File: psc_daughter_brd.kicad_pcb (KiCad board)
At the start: 2 copper layers, 50 x 150 mm, 144 parts, among them J1 61082-061400LF, U1 AD797, U11 ADR1001AEZ, U12 AD8221, U13 OPA277, U14 AD8221, U15 OPA277, U16 AD8221, U17 OPA277, U18 AD8221, U19 OPA277, U2 AD8676xR, U20 ADS8568SPM, U3 AD8676xR, U4 OPA277, U5 BUF634AxD, U6 AD5791BRUZ, U7 OPA277, U8 BUF634AxD, U9 OPA277

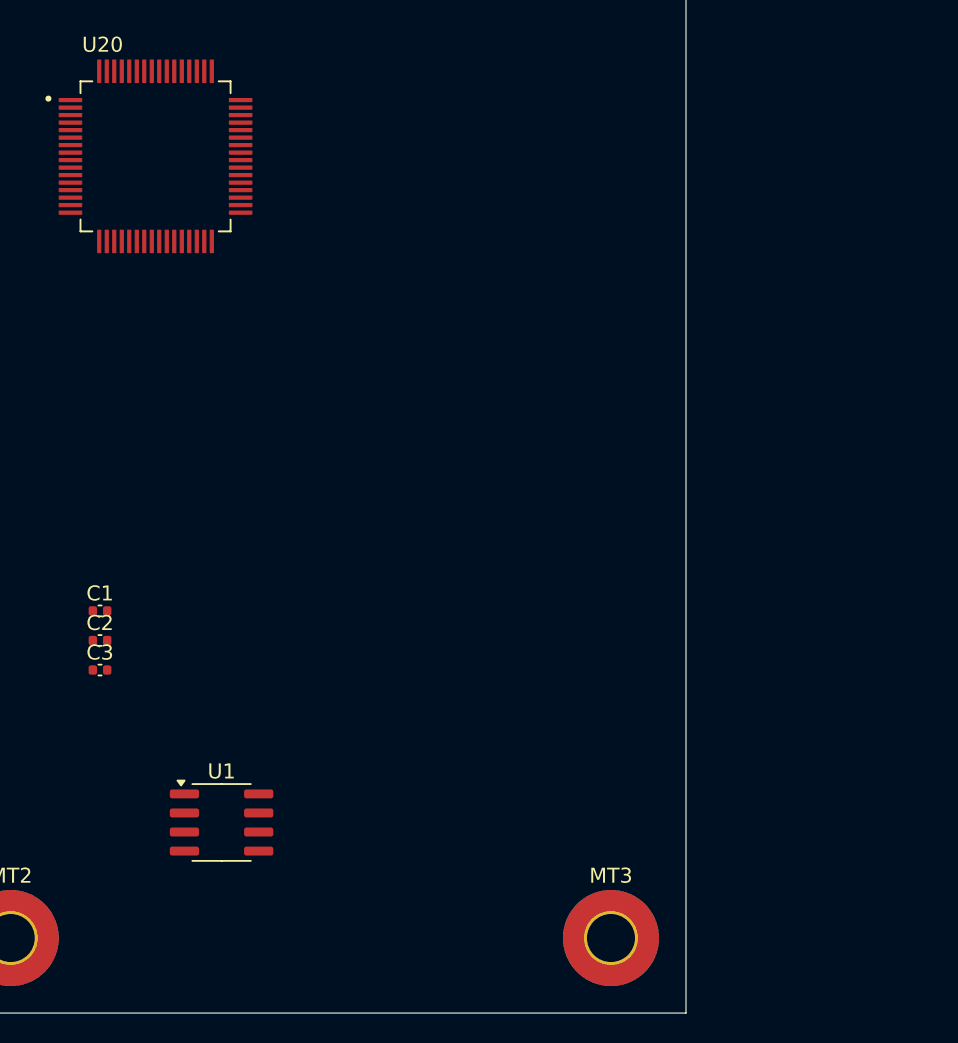
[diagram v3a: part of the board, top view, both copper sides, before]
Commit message: Add isolated digital I/O
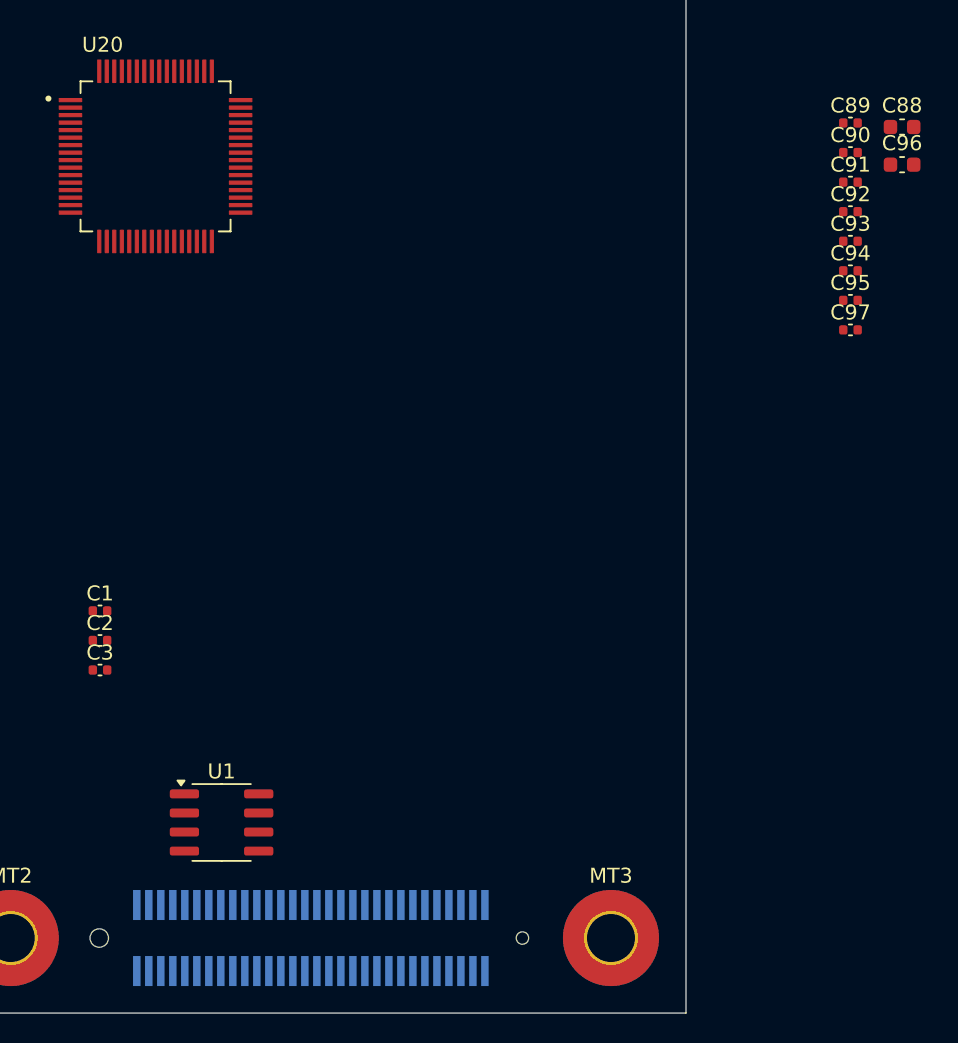
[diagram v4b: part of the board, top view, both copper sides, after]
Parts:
- added C88: 10uF, Capacitor_SMD:C_0603_1608Metric, F.Cu at (204.1, 132.7)
- added C89: 0.1uF, Capacitor_SMD:C_0402_1005Metric, F.Cu at (200.7, 132.5)
- added C90: 0.1uF, Capacitor_SMD:C_0402_1005Metric, F.Cu at (200.7, 134.4)
- added C91: 0.1uF, Capacitor_SMD:C_0402_1005Metric, F.Cu at (200.7, 136.4)
- added C92: 0.1uF, Capacitor_SMD:C_0402_1005Metric, F.Cu at (200.7, 138.4)
- added C93: 0.1uF, Capacitor_SMD:C_0402_1005Metric, F.Cu at (200.7, 140.3)
- added C94: 0.1uF, Capacitor_SMD:C_0402_1005Metric, F.Cu at (200.7, 142.3)
- added C95: 0.1uF, Capacitor_SMD:C_0402_1005Metric, F.Cu at (200.7, 144.3)
- added C96: 10uF, Capacitor_SMD:C_0603_1608Metric, F.Cu at (204.1, 135.2)
- added C97: 0.1uF, Capacitor_SMD:C_0402_1005Metric, F.Cu at (200.7, 146.2)
- added J2: 61082-061400LF, myparts:AMPHENOL_61082-061400LF, B.Cu at (164.7, 46.8)
- moved J1 140.0 mm to (164.7, 186.8)
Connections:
- net /DAC/SCLK renamed /DAC/sclk
- net /DAC/SDIN renamed /DAC/sdin
- net /DAC/SYNCN renamed /DAC/syncn
- U20 pad 10: unconnected-(U20-RESET-Pad10) -> /Monitor/reset
- U20 pad 11: unconnected-(U20-REFEN/~{WR}-Pad11) -> +3.3V
- U20 pad 12: unconnected-(U20-~{RD}-Pad12) -> GND
- U20 pad 13: unconnected-(U20-~{CS}/FS-Pad13) -> /Monitor/fs
- U20 pad 14: unconnected-(U20-AVDD-Pad14) -> Net-(C90-Pad1)
- U20 pad 15: unconnected-(U20-AGND-Pad15) -> GND
- U20 pad 16: unconnected-(U20-DB15/SDO_D-Pad16) -> GND
- U20 pad 17: unconnected-(U20-DB14/SDO_C-Pad17) -> GND
- U20 pad 18: unconnected-(U20-DB13/SDO_B-Pad18) -> GND
- U20 pad 19: unconnected-(U20-DB12/SDO_A-Pad19) -> /Monitor/sdo
- U20 pad 20: unconnected-(U20-DB11/~{REFBUFEN}-Pad20) -> GND
- U20 pad 21: unconnected-(U20-DB10/SCLK-Pad21) -> /Monitor/sclk
- U20 pad 22: unconnected-(U20-DB9/SDI-Pad22) -> GND
- U20 pad 23: unconnected-(U20-DB8/DCEN-Pad23) -> GND
- U20 pad 24: unconnected-(U20-DGND-Pad24) -> GND
- U20 pad 25: unconnected-(U20-DVDD-Pad25) -> +3.3V
- U20 pad 26: unconnected-(U20-DB7-Pad26) -> GND
- U20 pad 27: unconnected-(U20-DB6/SEL_B-Pad27) -> GND
- U20 pad 28: unconnected-(U20-DB5/SEL_CD-Pad28) -> GND
- U20 pad 29: unconnected-(U20-DB4-Pad29) -> GND
- U20 pad 30: unconnected-(U20-DB3/DCIN_A-Pad30) -> GND
- U20 pad 31: unconnected-(U20-DB2/DCIN_B-Pad31) -> GND
- U20 pad 32: unconnected-(U20-DB1/DCIN_C-Pad32) -> GND
- U20 pad 33: unconnected-(U20-DB0/DCIN_D-Pad33) -> GND
- U20 pad 34: unconnected-(U20-RANGE/XCLK-Pad34) -> GND
- U20 pad 35: unconnected-(U20-BUSY/INT-Pad35) -> /Monitor/busy
- U20 pad 36: unconnected-(U20-ASLEEP-Pad36) -> GND
- U20 pad 37: unconnected-(U20-CONVST_A-Pad37) -> /Monitor/convert
- U20 pad 38: unconnected-(U20-CONVST_B-Pad38) -> /Monitor/convert
- U20 pad 39: unconnected-(U20-CONVST_C-Pad39) -> /Monitor/convert
- U20 pad 4: unconnected-(U20-AVDD-Pad4) -> Net-(C90-Pad1)
- U20 pad 40: unconnected-(U20-CONVST_D-Pad40) -> /Monitor/convert
- U20 pad 41: unconnected-(U20-~{HW}/SW-Pad41) -> GND
- U20 pad 44: unconnected-(U20-AGND-Pad44) -> GND
- U20 pad 45: unconnected-(U20-AVDD-Pad45) -> Net-(C90-Pad1)
- U20 pad 48: unconnected-(U20-HVDD-Pad48) -> +15V
- U20 pad 5: unconnected-(U20-AGND-Pad5) -> GND
- U20 pad 51: unconnected-(U20-AGND-Pad51) -> GND
- U20 pad 52: unconnected-(U20-AVDD-Pad52) -> Net-(C90-Pad1)
- U20 pad 57: unconnected-(U20-AVDD-Pad57) -> Net-(C90-Pad1)
- U20 pad 58: unconnected-(U20-AGND-Pad58) -> GND
- U20 pad 61: unconnected-(U20-AVDD-Pad61) -> Net-(C90-Pad1)
- U20 pad 62: unconnected-(U20-AGND-Pad62) -> GND
- U20 pad 8: unconnected-(U20-~{PAR}/SER-Pad8) -> +3.3V
- U20 pad 9: unconnected-(U20-~{STBY}-Pad9) -> +3.3V

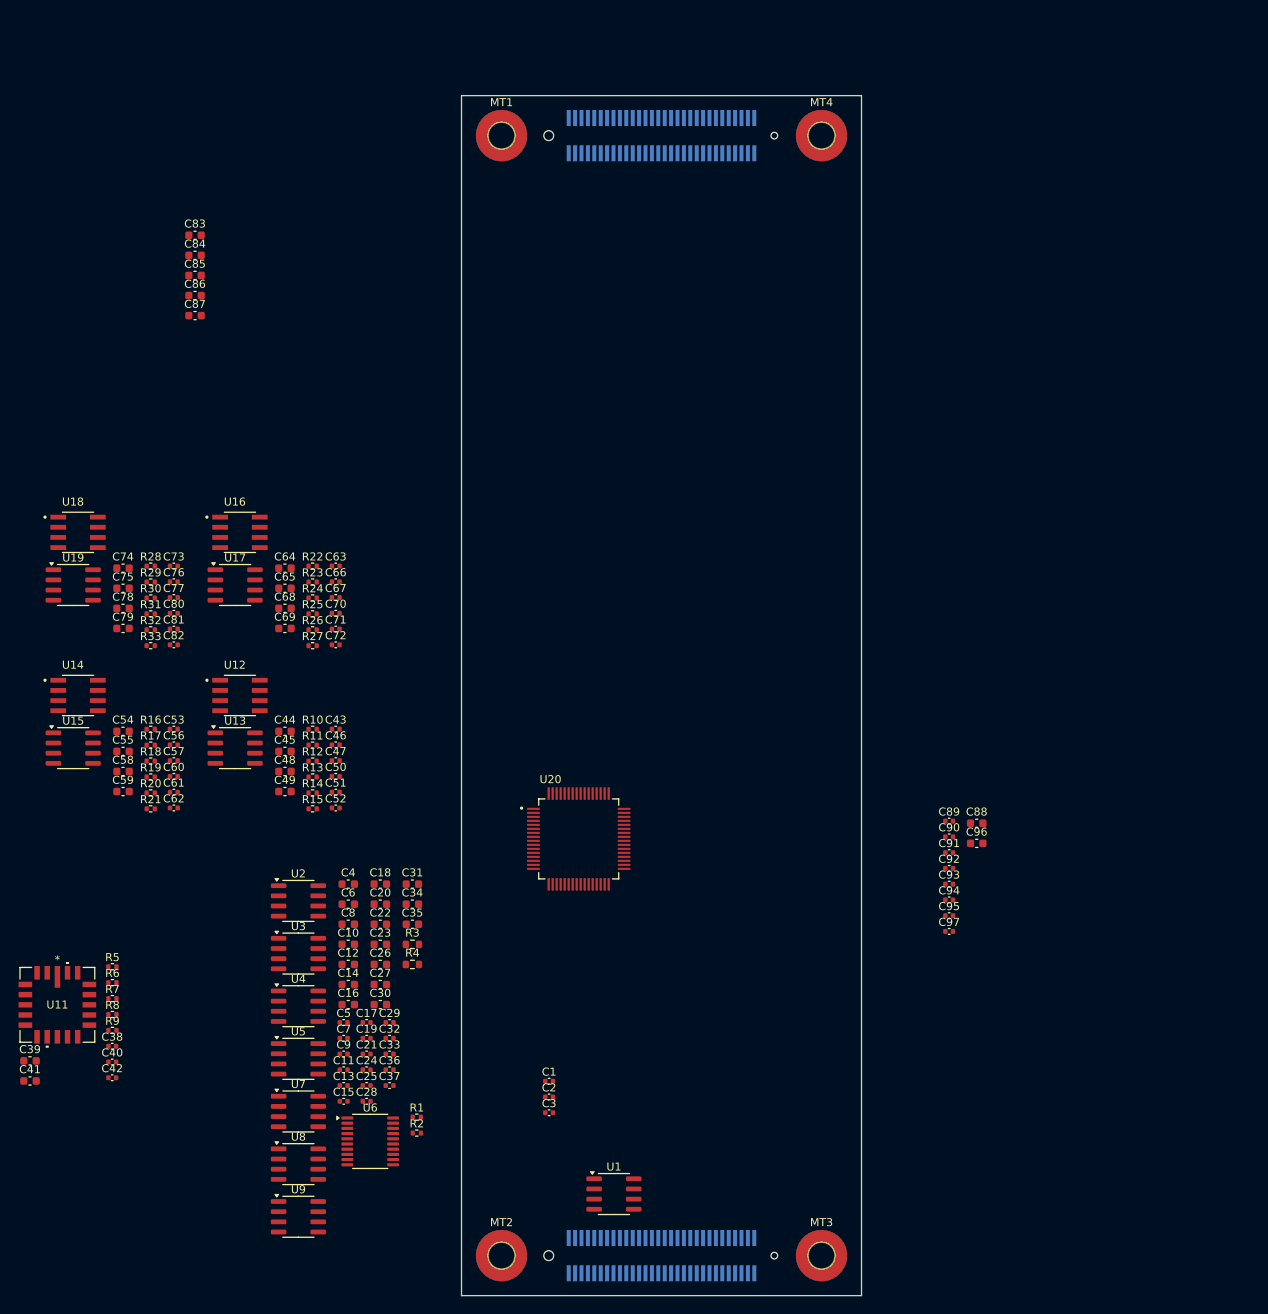
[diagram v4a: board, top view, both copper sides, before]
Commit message: Add DCCT ADCs
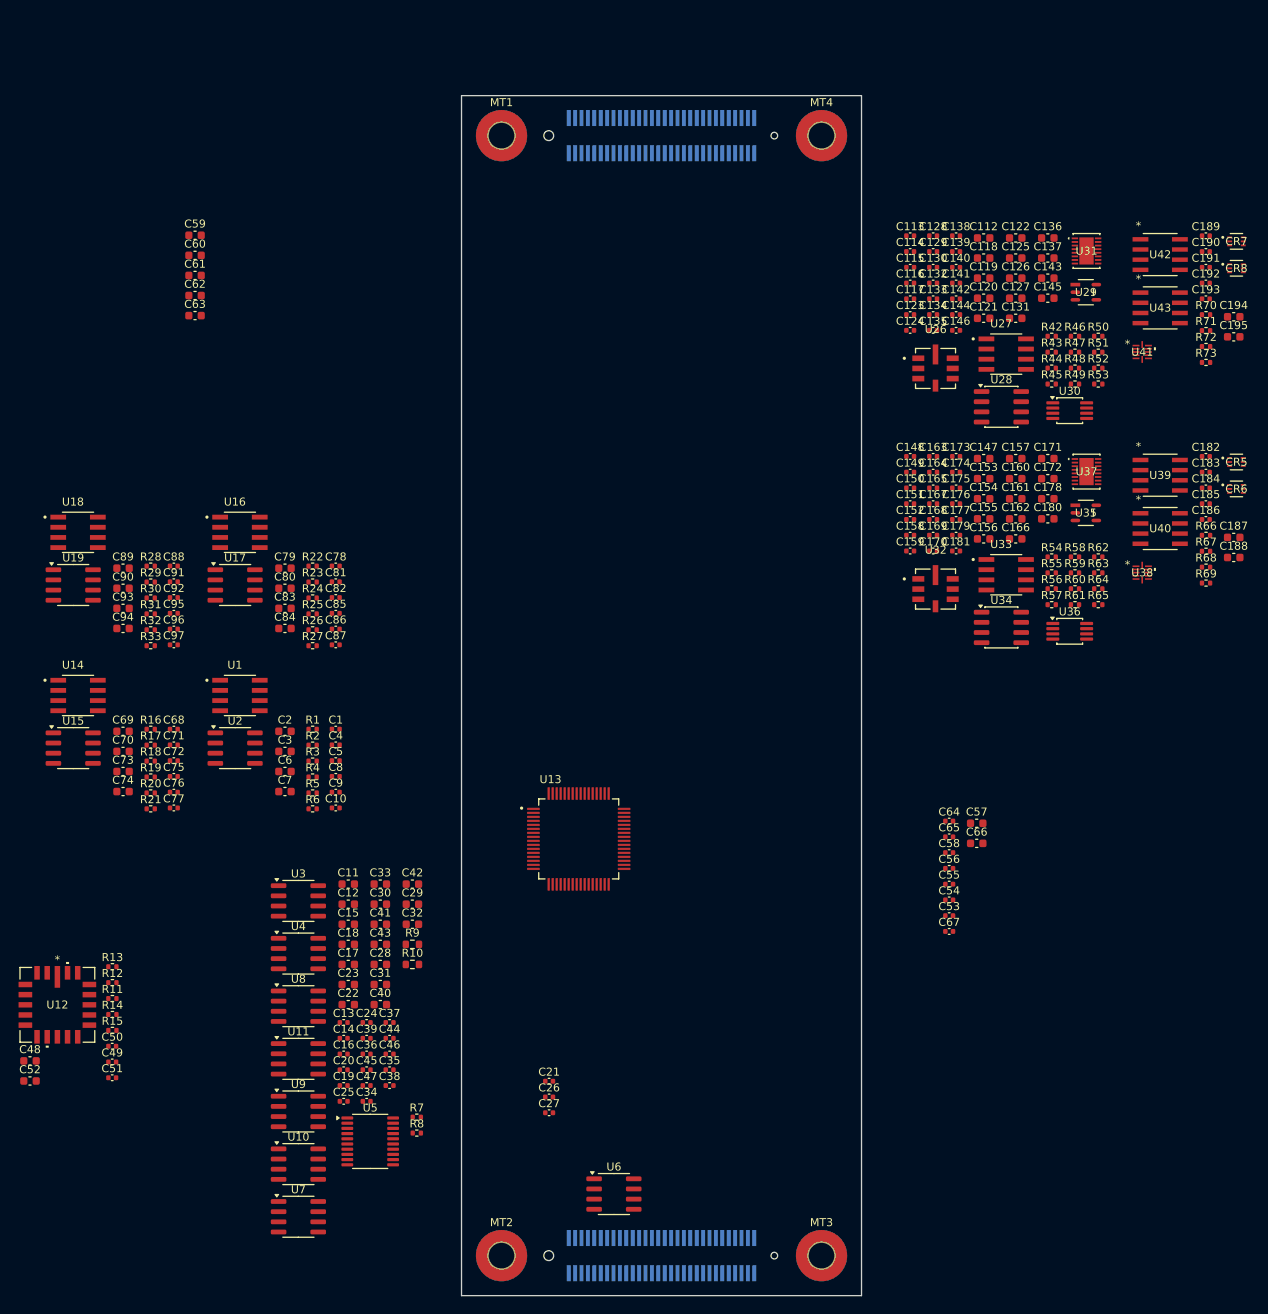
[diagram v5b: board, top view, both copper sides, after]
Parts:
- added C112: 10uF, Capacitor_SMD:C_0603_1608Metric, F.Cu at (205.0, 59.6)
- added C113: 0.1uF, Capacitor_SMD:C_0402_1005Metric, F.Cu at (195.8, 59.3)
- added C114: 6800pF, Capacitor_SMD:C_0402_1005Metric, F.Cu at (195.8, 61.3)
- added C115: 6800pF, Capacitor_SMD:C_0402_1005Metric, F.Cu at (195.8, 63.2)
- added C116: 3300pF, Capacitor_SMD:C_0402_1005Metric, F.Cu at (195.8, 65.2)
- added C117: 0.1uF, Capacitor_SMD:C_0402_1005Metric, F.Cu at (195.8, 67.2)
- added C118: 10uF, Capacitor_SMD:C_0603_1608Metric, F.Cu at (205.0, 62.1)
- added C119: 10uF, Capacitor_SMD:C_0603_1608Metric, F.Cu at (205.0, 64.6)
- added C120: 10uF, Capacitor_SMD:C_0603_1608Metric, F.Cu at (205.0, 67.1)
- added C121: 10uF, Capacitor_SMD:C_0603_1608Metric, F.Cu at (205.0, 69.6)
- added C122: 10uF, Capacitor_SMD:C_0603_1608Metric, F.Cu at (209.0, 59.6)
- added C123: 0.1uF, Capacitor_SMD:C_0402_1005Metric, F.Cu at (195.8, 69.1)
- added C124: 0.01uF, Capacitor_SMD:C_0402_1005Metric, F.Cu at (195.8, 71.1)
- added C125: 10uF, Capacitor_SMD:C_0603_1608Metric, F.Cu at (209.0, 62.1)
- added C126: 10uF, Capacitor_SMD:C_0603_1608Metric, F.Cu at (209.0, 64.6)
- added C127: 10uF, Capacitor_SMD:C_0603_1608Metric, F.Cu at (209.0, 67.1)
- added C128: 0.1uF, Capacitor_SMD:C_0402_1005Metric, F.Cu at (198.7, 59.3)
- added C129: 0.1uF, Capacitor_SMD:C_0402_1005Metric, F.Cu at (198.7, 61.3)
- added C130: 0.1uF, Capacitor_SMD:C_0402_1005Metric, F.Cu at (198.7, 63.2)
- added C131: 10uF, Capacitor_SMD:C_0603_1608Metric, F.Cu at (209.0, 69.6)
- added C132: 6800pF, Capacitor_SMD:C_0402_1005Metric, F.Cu at (198.7, 65.2)
- added C133: 3300pF, Capacitor_SMD:C_0402_1005Metric, F.Cu at (198.7, 67.2)
- added C134: 6800pF, Capacitor_SMD:C_0402_1005Metric, F.Cu at (198.7, 69.1)
- added C135: 0.1uF, Capacitor_SMD:C_0402_1005Metric, F.Cu at (198.7, 71.1)
- added C136: 10uF, Capacitor_SMD:C_0603_1608Metric, F.Cu at (213.0, 59.6)
- added C137: 10uF, Capacitor_SMD:C_0603_1608Metric, F.Cu at (213.0, 62.1)
- added C138: 0.1uF, Capacitor_SMD:C_0402_1005Metric, F.Cu at (201.5, 59.3)
- added C139: 0.1uF, Capacitor_SMD:C_0402_1005Metric, F.Cu at (201.5, 61.3)
- added C140: 6800pF, Capacitor_SMD:C_0402_1005Metric, F.Cu at (201.5, 63.2)
- added C141: 3300pF, Capacitor_SMD:C_0402_1005Metric, F.Cu at (201.5, 65.2)
- added C142: 6800pF, Capacitor_SMD:C_0402_1005Metric, F.Cu at (201.5, 67.2)
- added C143: 10uF, Capacitor_SMD:C_0603_1608Metric, F.Cu at (213.0, 64.6)
- added C144: 0.1uF, Capacitor_SMD:C_0402_1005Metric, F.Cu at (201.5, 69.1)
- added C145: 10uF, Capacitor_SMD:C_0603_1608Metric, F.Cu at (213.0, 67.1)
- added C146: 0.1uF, Capacitor_SMD:C_0402_1005Metric, F.Cu at (201.5, 71.1)
- added C147: 10uF, Capacitor_SMD:C_0603_1608Metric, F.Cu at (205.0, 87.1)
- added C148: 0.1uF, Capacitor_SMD:C_0402_1005Metric, F.Cu at (195.8, 86.9)
- added C149: 6800pF, Capacitor_SMD:C_0402_1005Metric, F.Cu at (195.8, 88.8)
- added C150: 6800pF, Capacitor_SMD:C_0402_1005Metric, F.Cu at (195.8, 90.8)
- added C151: 3300pF, Capacitor_SMD:C_0402_1005Metric, F.Cu at (195.8, 92.8)
- added C152: 0.1uF, Capacitor_SMD:C_0402_1005Metric, F.Cu at (195.8, 94.8)
- added C153: 10uF, Capacitor_SMD:C_0603_1608Metric, F.Cu at (205.0, 89.7)
- added C154: 10uF, Capacitor_SMD:C_0603_1608Metric, F.Cu at (205.0, 92.2)
- added C155: 10uF, Capacitor_SMD:C_0603_1608Metric, F.Cu at (205.0, 94.7)
- added C156: 10uF, Capacitor_SMD:C_0603_1608Metric, F.Cu at (205.0, 97.2)
- added C157: 10uF, Capacitor_SMD:C_0603_1608Metric, F.Cu at (209.0, 87.1)
- added C158: 0.1uF, Capacitor_SMD:C_0402_1005Metric, F.Cu at (195.8, 96.7)
- added C159: 0.01uF, Capacitor_SMD:C_0402_1005Metric, F.Cu at (195.8, 98.7)
- added C160: 10uF, Capacitor_SMD:C_0603_1608Metric, F.Cu at (209.0, 89.7)
- added C161: 10uF, Capacitor_SMD:C_0603_1608Metric, F.Cu at (209.0, 92.2)
- added C162: 10uF, Capacitor_SMD:C_0603_1608Metric, F.Cu at (209.0, 94.7)
- added C163: 0.1uF, Capacitor_SMD:C_0402_1005Metric, F.Cu at (198.7, 86.9)
- added C164: 0.1uF, Capacitor_SMD:C_0402_1005Metric, F.Cu at (198.7, 88.8)
- added C165: 0.1uF, Capacitor_SMD:C_0402_1005Metric, F.Cu at (198.7, 90.8)
- added C166: 10uF, Capacitor_SMD:C_0603_1608Metric, F.Cu at (209.0, 97.2)
- added C167: 6800pF, Capacitor_SMD:C_0402_1005Metric, F.Cu at (198.7, 92.8)
- added C168: 3300pF, Capacitor_SMD:C_0402_1005Metric, F.Cu at (198.7, 94.8)
- added C169: 6800pF, Capacitor_SMD:C_0402_1005Metric, F.Cu at (198.7, 96.7)
- added C170: 0.1uF, Capacitor_SMD:C_0402_1005Metric, F.Cu at (198.7, 98.7)
- added C171: 10uF, Capacitor_SMD:C_0603_1608Metric, F.Cu at (213.0, 87.1)
- added C172: 10uF, Capacitor_SMD:C_0603_1608Metric, F.Cu at (213.0, 89.7)
- added C173: 0.1uF, Capacitor_SMD:C_0402_1005Metric, F.Cu at (201.5, 86.9)
- added C174: 0.1uF, Capacitor_SMD:C_0402_1005Metric, F.Cu at (201.5, 88.8)
- added C175: 6800pF, Capacitor_SMD:C_0402_1005Metric, F.Cu at (201.5, 90.8)
- added C176: 3300pF, Capacitor_SMD:C_0402_1005Metric, F.Cu at (201.5, 92.8)
- added C177: 6800pF, Capacitor_SMD:C_0402_1005Metric, F.Cu at (201.5, 94.8)
- added C178: 10uF, Capacitor_SMD:C_0603_1608Metric, F.Cu at (213.0, 92.2)
- added C179: 0.1uF, Capacitor_SMD:C_0402_1005Metric, F.Cu at (201.5, 96.7)
- added C180: 10uF, Capacitor_SMD:C_0603_1608Metric, F.Cu at (213.0, 94.7)
- added C181: 0.1uF, Capacitor_SMD:C_0402_1005Metric, F.Cu at (201.5, 98.7)
- added C182: 0.1uF, Capacitor_SMD:C_0402_1005Metric, F.Cu at (232.7, 86.9)
- added C183: 0.1uF, Capacitor_SMD:C_0402_1005Metric, F.Cu at (232.7, 88.8)
- added C184: 0.1uF, Capacitor_SMD:C_0402_1005Metric, F.Cu at (232.7, 90.8)
- added C185: 0.1uF, Capacitor_SMD:C_0402_1005Metric, F.Cu at (232.7, 92.8)
- added C186: 0.1uF, Capacitor_SMD:C_0402_1005Metric, F.Cu at (232.7, 94.8)
- added C187: 10uF, Capacitor_SMD:C_0603_1608Metric, F.Cu at (236.2, 97.0)
- added C188: 10uF, Capacitor_SMD:C_0603_1608Metric, F.Cu at (236.2, 99.5)
- added C189: 0.1uF, Capacitor_SMD:C_0402_1005Metric, F.Cu at (232.7, 59.3)
- added C190: 0.1uF, Capacitor_SMD:C_0402_1005Metric, F.Cu at (232.7, 61.3)
- added C191: 0.1uF, Capacitor_SMD:C_0402_1005Metric, F.Cu at (232.7, 63.2)
- added C192: 0.1uF, Capacitor_SMD:C_0402_1005Metric, F.Cu at (232.7, 65.2)
- added C193: 0.1uF, Capacitor_SMD:C_0402_1005Metric, F.Cu at (232.7, 67.2)
- added C194: 10uF, Capacitor_SMD:C_0603_1608Metric, F.Cu at (236.2, 69.4)
- added C195: 10uF, Capacitor_SMD:C_0603_1608Metric, F.Cu at (236.2, 71.9)
- added CR5: SP3006-02XTG, myparts:SOT563_LTF, F.Cu at (236.6, 87.6)
- added CR6: SP3006-02XTG, myparts:SOT563_LTF, F.Cu at (236.6, 90.9)
- added CR7: SP3006-02XTG, myparts:SOT563_LTF, F.Cu at (236.6, 60.0)
- added CR8: SP3006-02XTG, myparts:SOT563_LTF, F.Cu at (236.6, 63.3)
- added R42: 1.0K, Resistor_SMD:R_0402_1005Metric, F.Cu at (213.5, 71.8)
- added R43: 1.0K, Resistor_SMD:R_0402_1005Metric, F.Cu at (213.5, 73.8)
- added R44: 665, Resistor_SMD:R_0402_1005Metric, F.Cu at (213.5, 75.8)
- added R45: 0, Resistor_SMD:R_0402_1005Metric, F.Cu at (213.5, 77.8)
- added R46: 1.3K, Resistor_SMD:R_0402_1005Metric, F.Cu at (216.4, 71.8)
- added R47: 10K, Resistor_SMD:R_0402_1005Metric, F.Cu at (216.4, 73.8)
- added R48: 10K, Resistor_SMD:R_0402_1005Metric, F.Cu at (216.4, 75.8)
- added R49: 10, Resistor_SMD:R_0402_1005Metric, F.Cu at (216.4, 77.8)
- added R50: 10, Resistor_SMD:R_0402_1005Metric, F.Cu at (219.3, 71.8)
- added R51: 15, Resistor_SMD:R_0402_1005Metric, F.Cu at (219.3, 73.8)
- added R52: 30.1, Resistor_SMD:R_0402_1005Metric, F.Cu at (219.3, 75.8)
- added R53: 30.1, Resistor_SMD:R_0402_1005Metric, F.Cu at (219.3, 77.8)
- added R54: 1.0K, Resistor_SMD:R_0402_1005Metric, F.Cu at (213.5, 99.4)
- added R55: 1.0K, Resistor_SMD:R_0402_1005Metric, F.Cu at (213.5, 101.4)
- added R56: 665, Resistor_SMD:R_0402_1005Metric, F.Cu at (213.5, 103.4)
- added R57: 0, Resistor_SMD:R_0402_1005Metric, F.Cu at (213.5, 105.4)
- added R58: 1.3K, Resistor_SMD:R_0402_1005Metric, F.Cu at (216.4, 99.4)
- added R59: 10K, Resistor_SMD:R_0402_1005Metric, F.Cu at (216.4, 101.4)
- added R60: 10K, Resistor_SMD:R_0402_1005Metric, F.Cu at (216.4, 103.4)
- added R61: 10, Resistor_SMD:R_0402_1005Metric, F.Cu at (216.4, 105.4)
- added R62: 10, Resistor_SMD:R_0402_1005Metric, F.Cu at (219.3, 99.4)
- added R63: 15, Resistor_SMD:R_0402_1005Metric, F.Cu at (219.3, 101.4)
- added R64: 30.1, Resistor_SMD:R_0402_1005Metric, F.Cu at (219.3, 103.4)
- added R65: 30.1, Resistor_SMD:R_0402_1005Metric, F.Cu at (219.3, 105.4)
- added R66: 2.49K, Resistor_SMD:R_0402_1005Metric, F.Cu at (232.8, 96.7)
- added R67: 2.49K, Resistor_SMD:R_0402_1005Metric, F.Cu at (232.8, 98.7)
- added R68: 2.49K, Resistor_SMD:R_0402_1005Metric, F.Cu at (232.8, 100.7)
- added R69: 2.49K, Resistor_SMD:R_0402_1005Metric, F.Cu at (232.8, 102.7)
- added R70: 2.49K, Resistor_SMD:R_0402_1005Metric, F.Cu at (232.8, 69.2)
- added R71: 2.49K, Resistor_SMD:R_0402_1005Metric, F.Cu at (232.8, 71.1)
- added R72: 2.49K, Resistor_SMD:R_0402_1005Metric, F.Cu at (232.8, 73.1)
- added R73: 2.49K, Resistor_SMD:R_0402_1005Metric, F.Cu at (232.8, 75.1)
- added U26: LTC6655BHLS8-5, myparts:LTC6655, F.Cu at (198.9, 75.9)
- added U27: AD8429BRZ, myparts:SOIC127P600X175-8N, F.Cu at (207.8, 74.1)
- added U28: AD8675ARZ, Package_SO:SOIC-8_3.9x4.9mm_P1.27mm, F.Cu at (207.2, 80.7)
- added U29: LT6202CS5, myparts:LT6202CS5, F.Cu at (217.7, 66.3)
- added U30: LTC6363xMS8, Package_SO:MSOP-8_3x3mm_P0.65mm, F.Cu at (215.7, 81.1)
- added U31: LTC2376CDE-20-PBF, myparts:DFN-16_DE_LIT, F.Cu at (217.8, 61.2)
- added U32: LTC6655BHLS8-5, myparts:LTC6655, F.Cu at (198.9, 103.5)
- added U33: AD8429BRZ, myparts:SOIC127P600X175-8N, F.Cu at (207.8, 101.7)
- added U34: AD8675ARZ, Package_SO:SOIC-8_3.9x4.9mm_P1.27mm, F.Cu at (207.2, 108.2)
- added U35: LT6202CS5, myparts:LT6202CS5, F.Cu at (217.7, 93.9)
- added U36: LTC6363xMS8, Package_SO:MSOP-8_3x3mm_P0.65mm, F.Cu at (215.7, 108.7)
- added U37: LTC2376CDE-20-PBF, myparts:DFN-16_DE_LIT, F.Cu at (217.8, 88.8)
- added U38: TXUN0104RUTR, myparts:PQFP12_RUT_TEX, F.Cu at (224.8, 101.4)
- added U39: ADUM5240ARZ, myparts:R_8_ADI, F.Cu at (227.0, 89.2)
- added U40: ADUM5240ARZ, myparts:R_8_ADI, F.Cu at (227.0, 95.9)
- added U41: TXUN0104RUTR, myparts:PQFP12_RUT_TEX, F.Cu at (224.8, 73.8)
- added U42: ADUM5242ARZ, myparts:R_8_ADI, F.Cu at (227.0, 61.6)
- added U43: ADUM5242ARZ, myparts:R_8_ADI, F.Cu at (227.0, 68.3)
- renumbered C43 to C1, C52 to C10, C4 to C11, C6 to C12, C5 to C13, C7 to C14, C8 to C15, C9 to C16, C12 to C17, C10 to C18, C13 to C19, C44 to C2, C11 to C20, C1 to C21, C16 to C22, C14 to C23, C17 to C24, C15 to C25, C2 to C26, C3 to C27, C26 to C28, C34 to C29, C45 to C3, C20 to C30, C27 to C31, C35 to C32, C18 to C33, C28 to C34, C36 to C35, C21 to C36, C29 to C37, C37 to C38, C19 to C39, C46 to C4, C30 to C40, C22 to C41, C31 to C42, C23 to C43, C32 to C44, C24 to C45, C33 to C46, C25 to C47, C39 to C48, C40 to C49, C47 to C5, C38 to C50, C42 to C51, C41 to C52, C95 to C53, C94 to C54, C93 to C55, C92 to C56, C88 to C57, C91 to C58, C83 to C59, C48 to C6, C84 to C60, C85 to C61, C86 to C62, C87 to C63, C89 to C64, C90 to C65, C96 to C66, C97 to C67, C53 to C68, C54 to C69, C49 to C7, C55 to C70, C56 to C71, C57 to C72, C58 to C73, C59 to C74, C60 to C75, C61 to C76, C62 to C77, C63 to C78, C64 to C79, C50 to C8, C65 to C80, C66 to C81, C67 to C82, C68 to C83, C69 to C84, C70 to C85, C71 to C86, C72 to C87, C73 to C88, C74 to C89, C51 to C9, C75 to C90, C76 to C91, C77 to C92, C78 to C93, C79 to C94, C80 to C95, C81 to C96, C82 to C97, J2 to J1, J1 to J2, R10 to R1, R4 to R10, R7 to R11, R6 to R12, R5 to R13, R8 to R14, R9 to R15, R11 to R2, R12 to R3, R13 to R4, R14 to R5, R15 to R6, R1 to R7, R2 to R8, R3 to R9, U12 to U1, U8 to U10, U5 to U11, U11 to U12, U20 to U13, U13 to U2, U2 to U3, U3 to U4, U6 to U5, U1 to U6, U9 to U7, U4 to U8, U7 to U9
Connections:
- net /Monitor/busy renamed /Monitor ADCs/busy
- net /Monitor/convert renamed /Monitor ADCs/convert
- net /Monitor/fs renamed /Monitor ADCs/fs
- net /Monitor/monitor_dac/mon_out renamed /Monitor ADCs/monitor_dac/mon_out
- net /Monitor/monitor_ignd/mon_out renamed /Monitor ADCs/monitor_ignd/mon_out
- net /Monitor/monitor_spare/mon_out renamed /Monitor ADCs/monitor_spare/mon_out
- net /Monitor/monitor_vout/mon_out renamed /Monitor ADCs/monitor_vout/mon_out
- net /Monitor/reset renamed /Monitor ADCs/reset
- net /Monitor/sclk renamed /Monitor ADCs/sclk
- net /Monitor/sdo renamed /Monitor ADCs/sdo
- J1 pad 1: (no net) -> unconnected-(J1-Pad1)
- J1 pad 10: (no net) -> unconnected-(J1-Pad10)
- J1 pad 11: (no net) -> unconnected-(J1-Pad11)
- J1 pad 12: (no net) -> /Isolated Digital IO/din0_iso
- J1 pad 13: (no net) -> unconnected-(J1-Pad13)
- J1 pad 14: (no net) -> /Isolated Digital IO/din1_iso
- J1 pad 15: (no net) -> unconnected-(J1-Pad15)
- J1 pad 16: (no net) -> /Isolated Digital IO/din2_iso
- J1 pad 17: (no net) -> unconnected-(J1-Pad17)
- J1 pad 18: (no net) -> /Isolated Digital IO/din3_iso
- J1 pad 19: (no net) -> unconnected-(J1-Pad19)
- J1 pad 2: (no net) -> /Isolated Digital IO/dout0_iso
- J1 pad 20: (no net) -> unconnected-(J1-Pad20)
- J1 pad 21: (no net) -> unconnected-(J1-Pad21)
- J1 pad 22: (no net) -> unconnected-(J1-Pad22)
- J1 pad 23: (no net) -> unconnected-(J1-Pad23)
- J1 pad 24: (no net) -> /Monitor ADCs/monitor_vout+
- J1 pad 25: (no net) -> unconnected-(J1-Pad25)
- J1 pad 26: (no net) -> /Monitor ADCs/monitor_vout-
- J1 pad 27: (no net) -> unconnected-(J1-Pad27)
- J1 pad 28: (no net) -> unconnected-(J1-Pad28)
- J1 pad 29: (no net) -> unconnected-(J1-Pad29)
- J1 pad 3: (no net) -> unconnected-(J1-Pad3)
- J1 pad 30: (no net) -> /Monitor ADCs/monitor_ignd+
- J1 pad 31: (no net) -> unconnected-(J1-Pad31)
- J1 pad 32: (no net) -> /Monitor ADCs/monitor_ignd-
- J1 pad 33: (no net) -> unconnected-(J1-Pad33)
- J1 pad 34: (no net) -> unconnected-(J1-Pad34)
- J1 pad 35: (no net) -> unconnected-(J1-Pad35)
- J1 pad 36: (no net) -> /Monitor ADCs/monitor_spare+
- J1 pad 37: (no net) -> unconnected-(J1-Pad37)
- J1 pad 38: (no net) -> /Monitor ADCs/monitor_spare-
- J1 pad 39: (no net) -> unconnected-(J1-Pad39)
- J1 pad 4: (no net) -> /Isolated Digital IO/dout1_iso
- J1 pad 40: (no net) -> unconnected-(J1-Pad40)
- J1 pad 41: (no net) -> unconnected-(J1-Pad41)
- J1 pad 42: (no net) -> /DAC/dac_out+
- J1 pad 43: (no net) -> unconnected-(J1-Pad43)
- J1 pad 44: (no net) -> /DAC/dac_vout-
- J1 pad 45: (no net) -> unconnected-(J1-Pad45)
- J1 pad 46: (no net) -> unconnected-(J1-Pad46)
- J1 pad 47: (no net) -> unconnected-(J1-Pad47)
- J1 pad 48: (no net) -> unconnected-(J1-Pad48)
- J1 pad 49: (no net) -> unconnected-(J1-Pad49)
- J1 pad 5: (no net) -> unconnected-(J1-Pad5)
- J1 pad 50: (no net) -> /DCCT ADCs/dcct0+
- J1 pad 51: (no net) -> unconnected-(J1-Pad51)
- J1 pad 52: (no net) -> /DCCT ADCs/dcct0-
- J1 pad 53: (no net) -> unconnected-(J1-Pad53)
- J1 pad 54: (no net) -> unconnected-(J1-Pad54)
- J1 pad 55: (no net) -> unconnected-(J1-Pad55)
- J1 pad 56: (no net) -> /DCCT ADCs/dcct1+
- J1 pad 57: (no net) -> unconnected-(J1-Pad57)
- J1 pad 58: (no net) -> /DCCT ADCs/dcct1-
- J1 pad 59: (no net) -> unconnected-(J1-Pad59)
- J1 pad 6: (no net) -> /Isolated Digital IO/dout2_iso
- J1 pad 60: (no net) -> unconnected-(J1-Pad60)
- J1 pad 7: (no net) -> unconnected-(J1-Pad7)
- J1 pad 8: (no net) -> /Isolated Digital IO/dout3_iso
- J1 pad 9: (no net) -> unconnected-(J1-Pad9)
- R1 pad 2: /Monitor/monitor_ignd+ -> /Monitor ADCs/monitor_ignd+
- R10 pad 2: /DAC/control_vout- -> /DAC/dac_vout-
- R16 pad 2: /Monitor/monitor_dac+ -> /DAC/dac_mon
- R17 pad 2: /Monitor/monitor_dac- -> GND
- R2 pad 2: /Monitor/monitor_ignd- -> /Monitor ADCs/monitor_ignd-
- R22 pad 2: /Monitor/monitor_spare+ -> /Monitor ADCs/monitor_spare+
- R23 pad 2: /Monitor/monitor_spare- -> /Monitor ADCs/monitor_spare-
- R28 pad 2: /Monitor/monitor_vout+ -> /Monitor ADCs/monitor_vout+
- R29 pad 2: /Monitor/monitor_vout- -> /Monitor ADCs/monitor_vout-
- R9 pad 2: /DAC/control_vout+ -> /DAC/dac_out+
